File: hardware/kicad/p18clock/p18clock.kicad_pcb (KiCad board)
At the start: 2 copper layers, 187.2 x 78.7 mm, 111 parts, among them J1 Conn_01x05_Pin, J2 Conn_01x05_Pin, J3 USB_C_Receptacle_PowerOnly_6P, J4 Conn_01x04_Pin, Q1 IRLML6401, Q2 IRLML6401, Q3 IRLML6401, Q4 IRLML6401, Q5 IRLML6401, Q6 IRLML6401, Q7 IRLML6401, Q8 IRLML6401, U1 74LS393, U10 KYX-1088B, U11 74HC164, U12 KYX-1088B, U13 LM35-LP, U14 PIC18F2550-ISO, U15 74LS148, U2 74HC138, U3 74HC164, U4 KYX-1088B, U5 74HC164, U6 KYX-1088B, U7 74HC164, U8 KYX-1088B, U9 74HC164, Y1 8MHz, Y2 32.768kHz

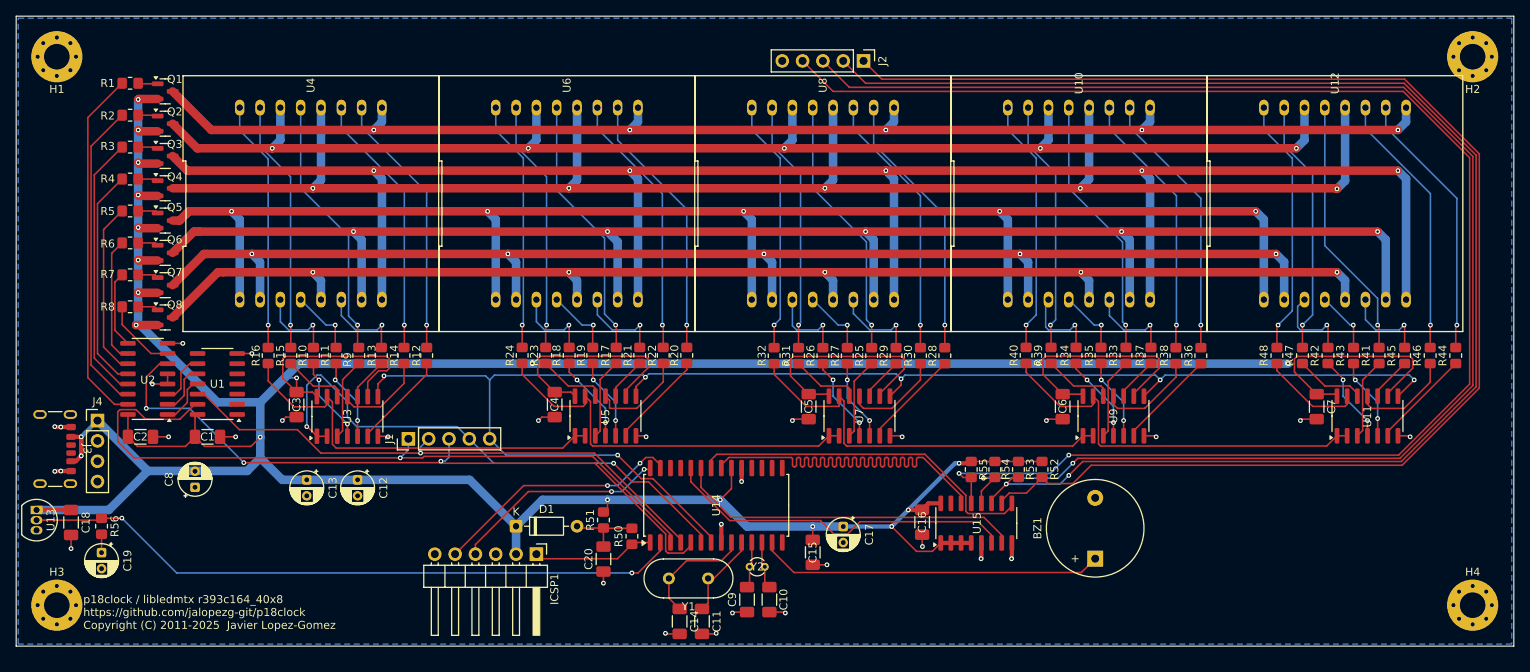
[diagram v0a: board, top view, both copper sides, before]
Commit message: p18clock/r393c164_40x8: fix defects in KiCad schematic / PCB
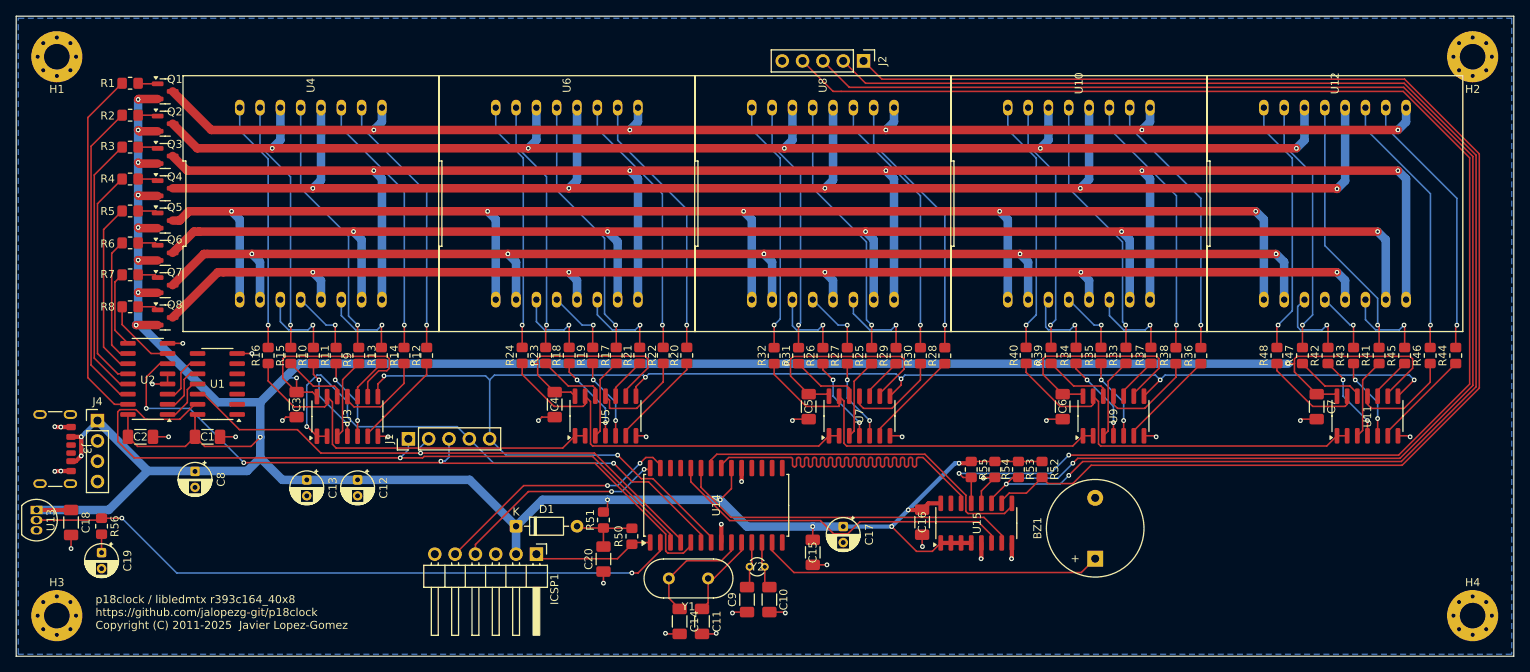
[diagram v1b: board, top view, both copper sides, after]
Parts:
- U1: value 74LS393 -> 74HC393
- U11, U3, U5, U7, U9: value 74HC164 -> 74HC164 / CD54ACT164
- moved C8 1.99 mm to (82.3, 118.9), turned to -90 degrees
- moved H3 1.31 mm to (65.0, 136.9)
- moved H4 1.31 mm to (242.0, 136.9)
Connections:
- C8 pad 1: GND -> VCC
- C8 pad 2: VCC -> GND
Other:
- board size 187.2 x 78.7 mm -> 187.2 x 80 mm

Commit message: [kicad] fix defects in KiCad schematic / PCB
Fix the following defects in KiCad schematic / PCB layout:
- Added 5k1 pull-down resistors in CC1 / CC2 USB-C pins
- Routed LM35.OUT signal on F.Cu layer s.t. it does not split B.Cu
  (GND) fill area
- Added F.Cu (GND) fill area
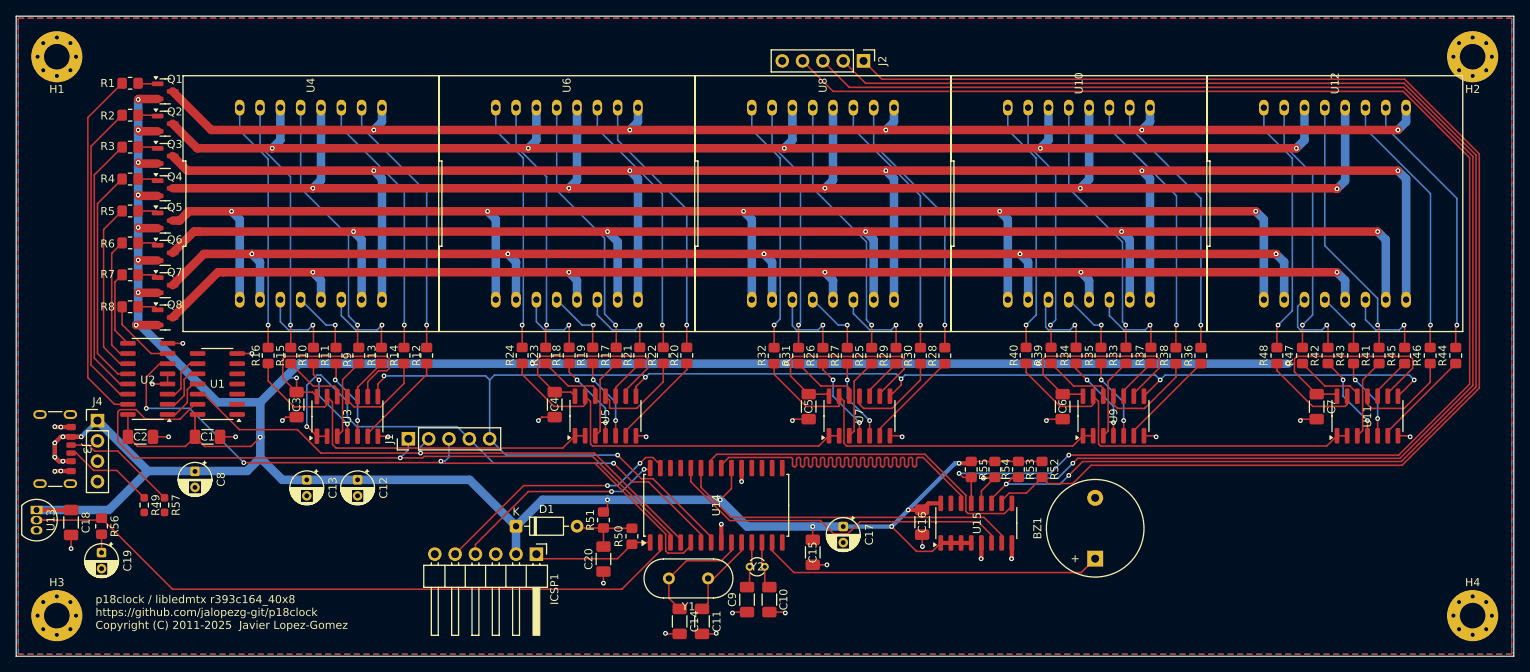
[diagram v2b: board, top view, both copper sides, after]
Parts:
- added R49: 5k1, Resistor_SMD:R_0603_1608Metric_Pad0.98x0.95mm_HandSolder, F.Cu at (75.9, 123.1)
- added R57: 5k1, Resistor_SMD:R_0603_1608Metric_Pad0.98x0.95mm_HandSolder, F.Cu at (78.5, 123.1)
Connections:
- J3 pad A5: unconnected-(J3-CC1-PadA5) -> Net-(J3-CC1)
- J3 pad B5: unconnected-(J3-CC2-PadB5) -> Net-(J3-CC2)
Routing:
- net Net-(J3-CC1): track 0.00 -> 14.4 mm
- net Net-(J3-CC2): track 0.00 -> 11.5 mm
- net VCC: track 570.2 -> 575.6 mm, vias 22 -> 25
- net Net-(U13-V_{OUT}): track 84.1 -> 85.8 mm, vias 2 -> 0
- added copper zone on F.Cu, net GND

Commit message: [hardware] Fix errata in XTAL capacitor values
Swap XTAL capacitors (8MHz should be 12-15pF; 32.768kHz should be
20-22pF).

Closes #23.
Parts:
- C10, C9: value 12pF -> 22pF
- C11, C14: value 22pF -> 12pF
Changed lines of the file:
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@@
 			)
 		)
-		(property "Value" "12pF"
+		(property "Value" "22pF"
 			(at 0 1.85 90)
 			(layer "F.Fab")
@@
 			)
 		)
-		(property "Value" "12pF"
+		(property "Value" "22pF"
 			(at 0 1.85 90)
 			(layer "F.Fab")
@@
 			)
 		)
-		(property "Value" "22pF"
+		(property "Value" "12pF"
 			(at 0 1.85 90)
 			(layer "F.Fab")
@@
 			)
 		)
-		(property "Value" "22pF"
+		(property "Value" "12pF"
 			(at 0 1.85 90)
 			(layer "F.Fab")
